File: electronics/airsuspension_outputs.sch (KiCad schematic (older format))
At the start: 51 parts, among them Q1 BSS138, Q2 BC847, U1 ITS5215L, U2 BTS6133D, U3 ITS5215L, U4 ITS5215L, U5 ITS5215L

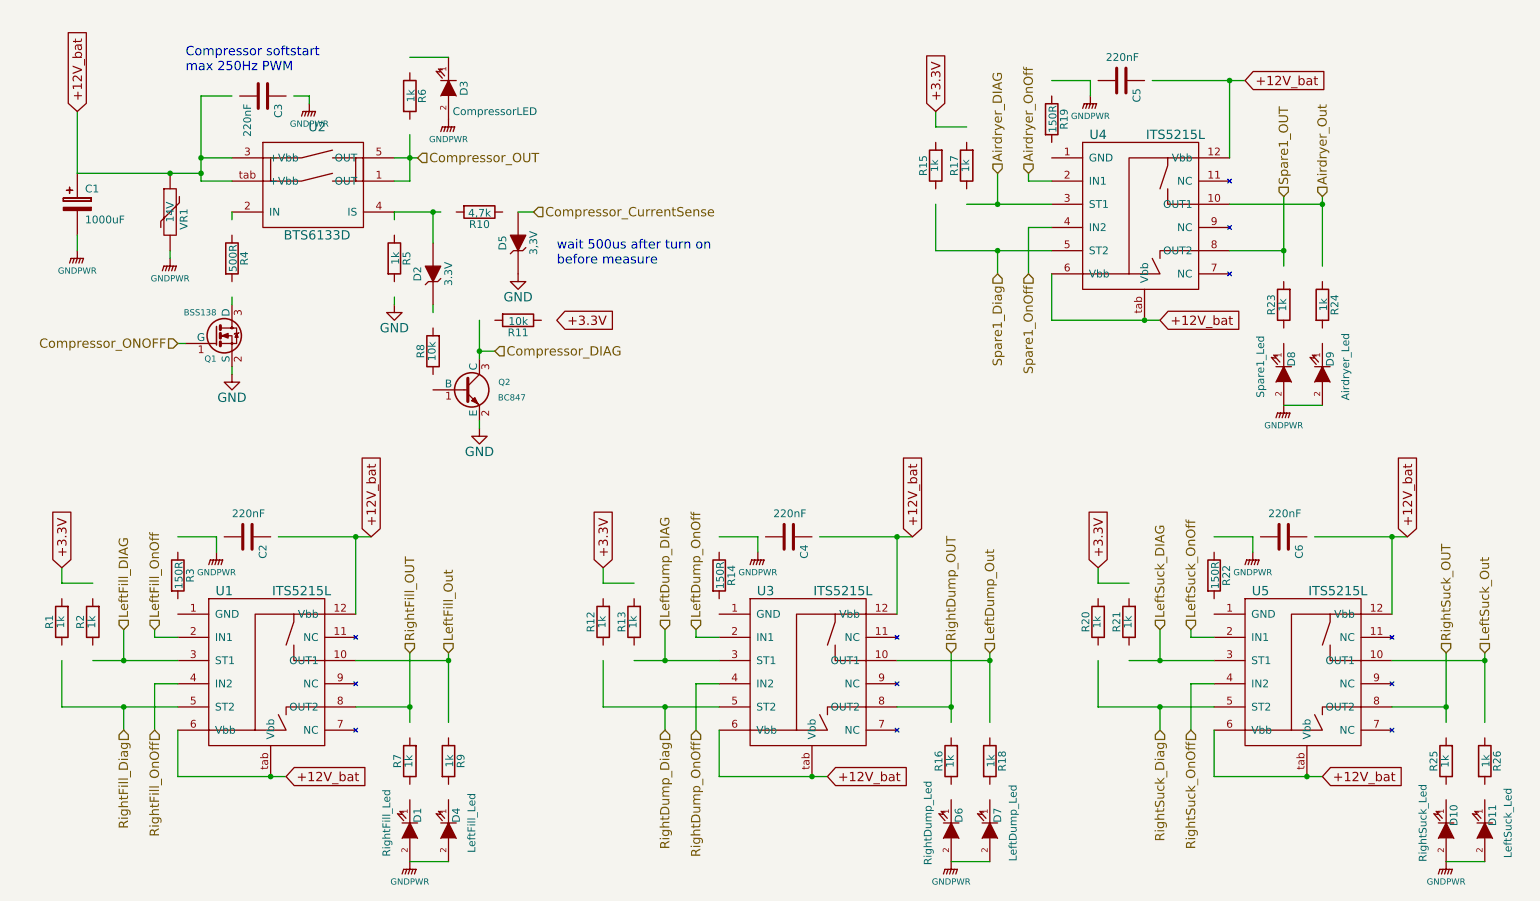
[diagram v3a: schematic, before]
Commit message: Changed to a more stable powersupply (3Amps 5V and separate 3.3v) + some few cleanups due to updated kicad
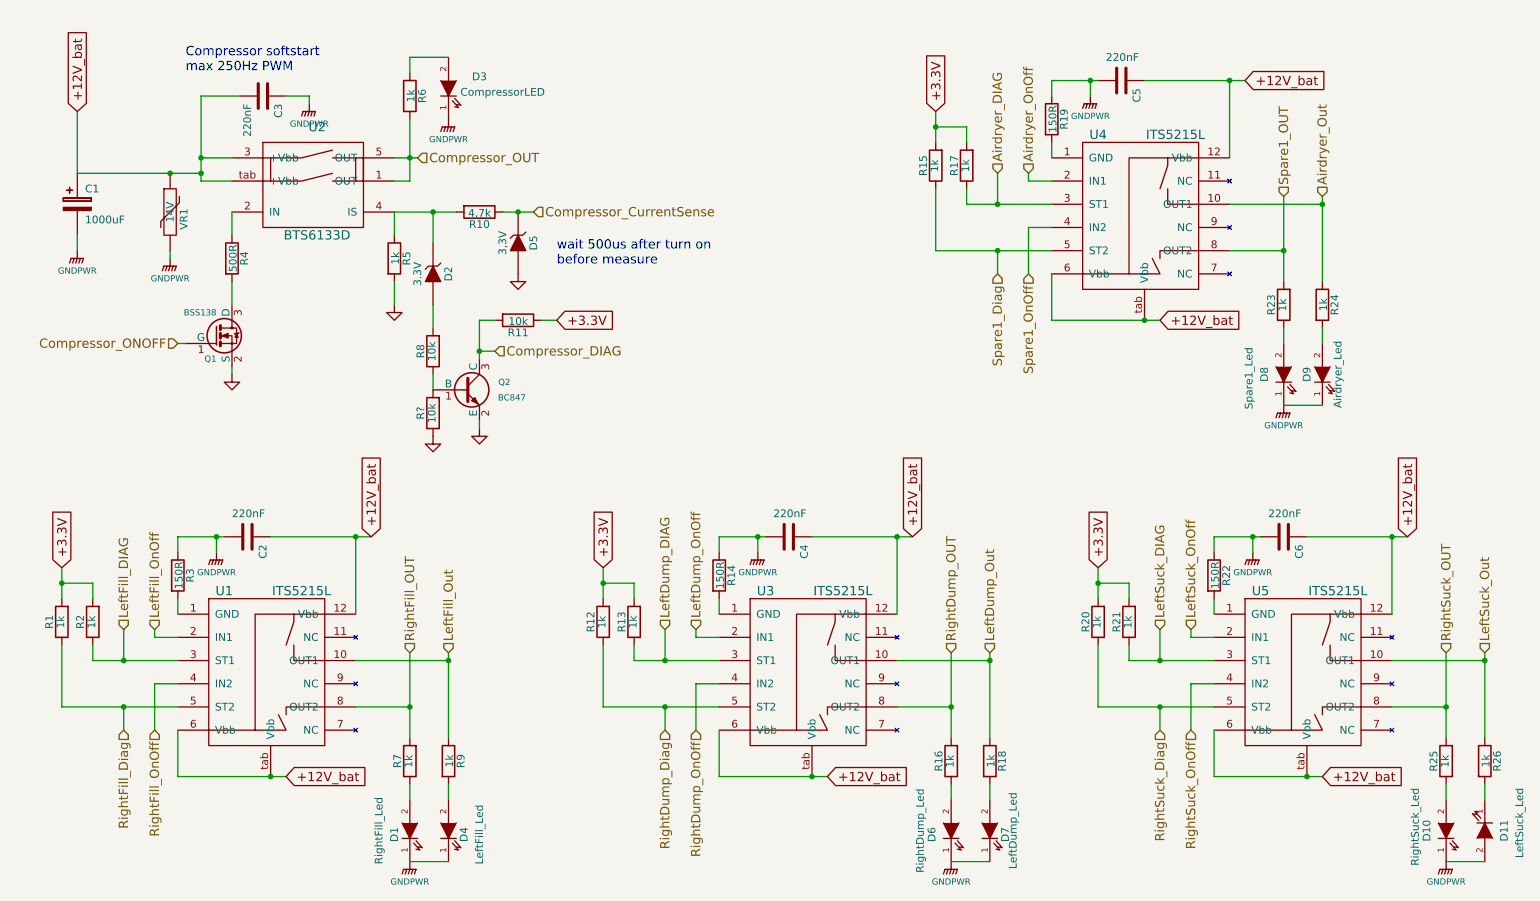
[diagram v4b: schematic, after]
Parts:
- added R?: 10k, Resistors_SMD:R_0805, symbol R
- U2: footprint SMD_Packages:DPAK-5 -> kicad_lib:bts6133d
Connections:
- wire segments 115 -> 143

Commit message: First placement with a ModICE enclosure
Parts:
- D1, D10, D11, D3, D4, D6, D7, D8, D9: footprint LEDs:LED-0805 -> LEDs:LED_0805
- Q1, Q2: footprint Housings_SOT-23_SOT-143_TSOT-6:SOT-23 -> TO_SOT_Packages_SMD:SOT-23_Handsoldering
- R54: renamed from R?; value 10k -> 1k; farnell 612522 -> 1577659; name CR0805-FX-1002ELF -> ERA6AEB102V
- R8: value 10k -> 1k; farnell 612522 -> 1577659; name CR0805-FX-1002ELF -> ERA6AEB102V
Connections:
- net GNDPWR: now also D11.1 (K); no longer D11.2 (A)
- net at R26.2: now also D11.2 (A); no longer D11.1 (K)
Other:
- note added: "wait 500us after turn on\nbefore current measure"
- note removed: "wait 500us after turn on\nbefore measure"
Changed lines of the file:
@@
 LIBS:power_switches
 LIBS:miscellaneous
+LIBS:cinch
 LIBS:airsuspension_controller-cache
 EELAYER 25 0
@@
 +12V_bat
 $Comp
-L GNDPWR #PWR06
+L GNDPWR #PWR07
 U 1 1 5504BD26
 P 3000 1150
-F 0 "#PWR06" H 3000 950 40  0001 C CNN
+F 0 "#PWR07" H 3000 950 40  0001 C CNN
 F 1 "GNDPWR" H 3000 1020 40  0000 C CNN
 F 2 "" H 3000 1100 60  0000 C CNN
@@
 $EndComp
 $Comp
-L GNDPWR #PWR07
+L GNDPWR #PWR08
 U 1 1 5504BD5A
 P 2100 2150
-F 0 "#PWR07" H 2100 1950 40  0001 C CNN
+F 0 "#PWR08" H 2100 1950 40  0001 C CNN
 F 1 "GNDPWR" H 2100 2020 40  0000 C CNN
 F 2 "" H 2100 2100 60  0000 C CNN
@@
 $EndComp
 $Comp
-L GNDPWR #PWR08
+L GNDPWR #PWR09
 U 1 1 5504BD7C
 P 1500 2100
-F 0 "#PWR08" H 1500 1900 40  0001 C CNN
+F 0 "#PWR09" H 1500 1900 40  0001 C CNN
 F 1 "GNDPWR" H 1500 1970 40  0000 C CNN
 F 2 "" H 1500 2050 60  0000 C CNN
@@
 $EndComp
 $Comp
-L GNDPWR #PWR09
+L GNDPWR #PWR010
 U 1 1 5504BE79
 P 2400 4050
-F 0 "#PWR09" H 2400 3850 40  0001 C CNN
+F 0 "#PWR010" H 2400 3850 40  0001 C CNN
 F 1 "GNDPWR" H 2400 3920 40  0000 C CNN
 F 2 "" H 2400 4000 60  0000 C CNN
@@
 $EndComp
 $Comp
-L GND #PWR010
+L GND #PWR011
 U 1 1 5504D3D3
 P 2500 2900
-F 0 "#PWR010" H 2500 2650 60  0001 C CNN
+F 0 "#PWR011" H 2500 2650 60  0001 C CNN
 F 1 "GND" H 2500 2750 60  0001 C CNN
 F 2 "" H 2500 2900 60  0000 C CNN
@@
 P 3800 2750
 F 0 "R8" V 3880 2750 50  0000 C CNN
-F 1 "10k" V 3807 2751 50  0000 C CNN
+F 1 "1k" V 3807 2751 50  0000 C CNN
 F 2 "Resistors_SMD:R_0805" V 3730 2750 30  0001 C CNN
 F 3 "" H 3800 2750 30  0000 C CNN
-F 4 "CR0805-FX-1002ELF" V 3800 2750 60  0001 C CNN "name"
-F 5 "612522" V 3800 2750 60  0001 C CNN "farnell"
+F 4 "ERA6AEB102V" V 3800 2750 60  0001 C CNN "name"
+F 5 "1577659" V 3800 2750 60  0001 C CNN "farnell"
 	1    3800 2750
 	-1   0    0    1
 $EndComp
 $Comp
-L GND #PWR011
+L GND #PWR012
 U 1 1 5504D6E9
 P 4100 3250
-F 0 "#PWR011" H 4100 3000 60  0001 C CNN
+F 0 "#PWR012" H 4100 3000 60  0001 C CNN
 F 1 "GND" H 4100 3100 60  0001 C CNN
 F 2 "" H 4100 3250 60  0000 C CNN
@@
 $EndComp
 $Comp
-L GND #PWR012
+L GND #PWR013
 U 1 1 5504D71D
 P 3550 2450
-F 0 "#PWR012" H 3550 2200 60  0001 C CNN
+F 0 "#PWR013" H 3550 2200 60  0001 C CNN
 F 1 "GND" H 3550 2300 60  0001 C CNN
 F 2 "" H 3550 2450 60  0000 C CNN
@@
 $EndComp
 $Comp
-L GND #PWR013
+L GND #PWR014
 U 1 1 5504DCBC
 P 4350 2250
-F 0 "#PWR013" H 4350 2000 60  0001 C CNN
+F 0 "#PWR014" H 4350 2000 60  0001 C CNN
 F 1 "GND" H 4350 2100 60  0001 C CNN
 F 2 "" H 4350 2250 60  0000 C CNN
@@
 F 0 "D3" V 3975 850 50  0000 C CNN
 F 1 "CompressorLED" V 3875 700 50  0000 C CNN
-F 2 "LEDs:LED-0805" H 3900 1050 60  0001 C CNN
+F 2 "LEDs:LED_0805" H 3900 1050 60  0001 C CNN
 F 3 "" H 3900 1050 60  0000 C CNN
 F 4 "KP-2012CGCK" H 3900 1050 60  0001 C CNN "name"
@@
 $EndComp
 $Comp
-L GNDPWR #PWR014
+L GNDPWR #PWR015
 U 1 1 5504E76C
 P 3900 1250
-F 0 "#PWR014" H 3900 1050 40  0001 C CNN
+F 0 "#PWR015" H 3900 1050 40  0001 C CNN
 F 1 "GNDPWR" H 3900 1120 40  0000 C CNN
 F 2 "" H 3900 1200 60  0000 C CNN
@@
 Compressor softstart\nmax 250Hz PWM
 Text Notes 4600 2200 0    60   ~ 0
-wait 500us after turn on\nbefore measure
+wait 500us after turn on\nbefore current measure
 $Comp
 L R R2
@@
 F 0 "D1" H 3625 5950 50  0000 C CNN
 F 1 "RightFill_Led" H 3650 6050 50  0000 C CNN
-F 2 "LEDs:LED-0805" H 3650 5850 60  0001 C CNN
+F 2 "LEDs:LED_0805" H 3650 5850 60  0001 C CNN
 F 3 "" H 3650 5850 60  0000 C CNN
 F 4 "KP-2012CGCK" H 3650 5850 60  0001 C CNN "name"
@@
 F 0 "D4" H 3875 5750 50  0000 C CNN
 F 1 "LeftFill_Led" H 3875 5650 50  0000 C CNN
-F 2 "LEDs:LED-0805" H 3900 5850 60  0001 C CNN
+F 2 "LEDs:LED_0805" H 3900 5850 60  0001 C CNN
 F 3 "" H 3900 5850 60  0000 C CNN
 F 4 "KP-2012CGCK" H 3900 5850 60  0001 C CNN "name"
@@
 $EndComp
 $Comp
-L GNDPWR #PWR015
+L GNDPWR #PWR016
 U 1 1 55050558
 P 3650 6050
-F 0 "#PWR015" H 3650 5850 40  0001 C CNN
+F 0 "#PWR016" H 3650 5850 40  0001 C CNN
 F 1 "GNDPWR" H 3650 5920 40  0000 C CNN
 F 2 "" H 3650 6000 60  0000 C CNN
@@
 $EndComp
 $Comp
-L GNDPWR #PWR016
+L GNDPWR #PWR017
 U 1 1 55056301
 P 8050 1100
-F 0 "#PWR016" H 8050 900 40  0001 C CNN
+F 0 "#PWR017" H 8050 900 40  0001 C CNN
 F 1 "GNDPWR" H 8050 970 40  0000 C CNN
 F 2 "" H 8050 1050 60  0000 C CNN
@@
 F 0 "D8" H 9300 3025 50  0000 C CNN
 F 1 "Spare1_Led" H 9275 3125 50  0000 C CNN
-F 2 "LEDs:LED-0805" H 9300 2900 60  0001 C CNN
+F 2 "LEDs:LED_0805" H 9300 2900 60  0001 C CNN
 F 3 "" H 9300 2900 60  0000 C CNN
 F 4 "2290331" H 9300 2900 60  0001 C CNN "farnell"
@@
 F 0 "D9" H 9550 3000 50  0000 C CNN
 F 1 "Airdryer_Led" H 9550 2800 50  0000 C CNN
-F 2 "LEDs:LED-0805" H 9550 2900 60  0001 C CNN
+F 2 "LEDs:LED_0805" H 9550 2900 60  0001 C CNN
 F 3 "" H 9550 2900 60  0000 C CNN
 F 4 "KP-2012CGCK" H 9550 2900 60  0001 C CNN "name"
@@
 $EndComp
 $Comp
-L GNDPWR #PWR017
+L GNDPWR #PWR018
 U 1 1 5505633E
 P 9300 3100
-F 0 "#PWR017" H 9300 2900 40  0001 C CNN
+F 0 "#PWR018" H 9300 2900 40  0001 C CNN
 F 1 "GNDPWR" H 9300 2970 40  0000 C CNN
 F 2 "" H 9300 3050 60  0000 C CNN
@@
 $EndComp
 $Comp
-L GNDPWR #PWR018
+L GNDPWR #PWR019
 U 1 1 5505681E
 P 9100 4050
-F 0 "#PWR018" H 9100 3850 40  0001 C CNN
+F 0 "#PWR019" H 9100 3850 40  0001 C CNN
 F 1 "GNDPWR" H 9100 3920 40  0000 C CNN
 F 2 "" H 9100 4000 60  0000 C CNN
@@
 F 0 "D10" H 10350 5975 50  0000 C CNN
 F 1 "RightSuck_Led" H 10375 6050 50  0000 C CNN
-F 2 "LEDs:LED-0805" H 10350 5850 60  0001 C CNN
+F 2 "LEDs:LED_0805" H 10350 5850 60  0001 C CNN
 F 3 "" H 10350 5850 60  0000 C CNN
 F 4 "2290331" H 10350 5850 60  0001 C CNN "farnell"
@@
 F 0 "D11" H 10600 5975 50  0000 C CNN
 F 1 "LeftSuck_Led" H 10550 6075 50  0000 C CNN
-F 2 "LEDs:LED-0805" H 10600 5850 60  0001 C CNN
+F 2 "LEDs:LED_0805" H 10600 5850 60  0001 C CNN
 F 3 "" H 10600 5850 60  0000 C CNN
 F 4 "KP-2012CGCK" H 10600 5850 60  0001 C CNN "name"
 F 5 "2290331" H 10600 5850 60  0001 C CNN "farnell"
 	1    10600 5850
-	0    1    1    0
-$EndComp
-$Comp
-L GNDPWR #PWR019
+	0    -1   -1   0
+$EndComp
+$Comp
+L GNDPWR #PWR020
 U 1 1 5505685B
 P 10350 6050
-F 0 "#PWR019" H 10350 5850 40  0001 C CNN
+F 0 "#PWR020" H 10350 5850 40  0001 C CNN
 F 1 "GNDPWR" H 10350 5920 40  0000 C CNN
 F 2 "" H 10350 6000 60  0000 C CNN
@@
 $EndComp
 $Comp
-L GNDPWR #PWR020
+L GNDPWR #PWR021
 U 1 1 55056A62
 P 5900 4050
-F 0 "#PWR020" H 5900 3850 40  0001 C CNN
+F 0 "#PWR021" H 5900 3850 40  0001 C CNN
 F 1 "GNDPWR" H 5900 3920 40  0000 C CNN
 F 2 "" H 5900 4000 60  0000 C CNN
@@
 F 0 "D6" H 7125 5975 50  0000 C CNN
 F 1 "RightDump_Led" H 7150 6050 50  0000 C CNN
-F 2 "LEDs:LED-0805" H 7150 5850 60  0001 C CNN
+F 2 "LEDs:LED_0805" H 7150 5850 60  0001 C CNN
 F 3 "" H 7150 5850 60  0000 C CNN
 F 4 "2290331" H 7150 5850 60  0001 C CNN "farnell"
@@
 F 0 "D7" H 7375 5750 50  0000 C CNN
 F 1 "LeftDump_Led" H 7400 5700 50  0000 C CNN
-F 2 "LEDs:LED-0805" H 7400 5850 60  0001 C CNN
+F 2 "LEDs:LED_0805" H 7400 5850 60  0001 C CNN
 F 3 "" H 7400 5850 60  0000 C CNN
 F 4 "KP-2012CGCK" H 7400 5850 60  0001 C CNN "name"
@@
 $EndComp
 $Comp
-L GNDPWR #PWR021
+L GNDPWR #PWR022
 U 1 1 55056A9F
 P 7150 6050
-F 0 "#PWR021" H 7150 5850 40  0001 C CNN
+F 0 "#PWR022" H 7150 5850 40  0001 C CNN
 F 1 "GNDPWR" H 7150 5920 40  0000 C CNN
 F 2 "" H 7150 6000 60  0000 C CNN
@@
 F 0 "Q2" H 4300 3050 40  0000 R CNN
 F 1 "BC847" H 4400 2950 40  0000 R CNN
-F 2 "Housings_SOT-23_SOT-143_TSOT-6:SOT-23" H 4250 2900 29  0001 C CNN
+F 2 "TO_SOT_Packages_SMD:SOT-23_Handsoldering" H 4250 2900 29  0001 C CNN
 F 3 "" H 4000 3000 60  0000 C CNN
 F 4 "1773609" H 4000 3000 60  0001 C CNN "farnell"
@@
 F 0 "Q1" H 2400 2501 40  0000 R CNN
 F 1 "BSS138" H 2400 2800 40  0000 R CNN
-F 2 "Housings_SOT-23_SOT-143_TSOT-6:SOT-23" H 2270 2752 29  0001 C CNN
+F 2 "TO_SOT_Packages_SMD:SOT-23_Handsoldering" H 2270 2752 29  0001 C CNN
 F 3 "" H 2400 2650 60  0000 C CNN
 F 4 "2053833" H 2400 2650 60  0001 C CNN "farnell"
@@
 	9300 2600 9300 2700
 $Comp
-L R R?
+L R R54
 U 1 1 56FAA483
 P 3800 3150
-F 0 "R?" V 3880 3150 50  0000 C CNN
-F 1 "10k" V 3807 3151 50  0000 C CNN
+F 0 "R54" V 3880 3150 50  0000 C CNN
+F 1 "1k" V 3807 3151 50  0000 C CNN
 F 2 "Resistors_SMD:R_0805" V 3730 3150 30  0001 C CNN
 F 3 "" H 3800 3150 30  0000 C CNN
-F 4 "CR0805-FX-1002ELF" V 3800 3150 60  0001 C CNN "name"
-F 5 "612522" V 3800 3150 60  0001 C CNN "farnell"
+F 4 "ERA6AEB102V" V 3800 3150 60  0001 C CNN "name"
+F 5 "1577659" V 3800 3150 60  0001 C CNN "farnell"
 	1    3800 3150
 	-1   0    0    1
 $EndComp
 $Comp
-L GND #PWR?
+L GND #PWR023
 U 1 1 56FAA639
 P 3800 3300
-F 0 "#PWR?" H 3800 3050 50  0001 C CNN
+F 0 "#PWR023" H 3800 3050 50  0001 C CNN
 F 1 "GND" H 3808 3127 50  0001 C CNN
 F 2 "" H 3800 3300 50  0000 C CNN

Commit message: PCB routing done
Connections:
- net GND: no longer Q1.2 (S)
- net GNDPWR: now also Q1.2 (S)
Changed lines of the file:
@@
-	1    0    0    -1
-$EndComp
-$Comp
-L GND #PWR011
-U 1 1 5504D3D3
-P 2500 2900
-F 0 "#PWR011" H 2500 2650 60  0001 C CNN
-F 1 "GND" H 2500 2750 60  0001 C CNN
-F 2 "" H 2500 2900 60  0000 C CNN
-F 3 "" H 2500 2900 60  0000 C CNN
-	1    2500 2900
 	1    0    0    -1
 $EndComp
@@
 	1    0    0    -1
 $EndComp
+$Comp
+L GNDPWR #PWR?
+U 1 1 5701DD89
+P 2500 2900
+F 0 "#PWR?" H 2500 2700 50  0001 C CNN
+F 1 "GNDPWR" H 2507 2974 50  0001 C CNN
+F 2 "" H 2500 2850 50  0000 C CNN
+F 3 "" H 2500 2850 50  0000 C CNN
+	1    2500 2900
+	1    0    0    -1
+$EndComp

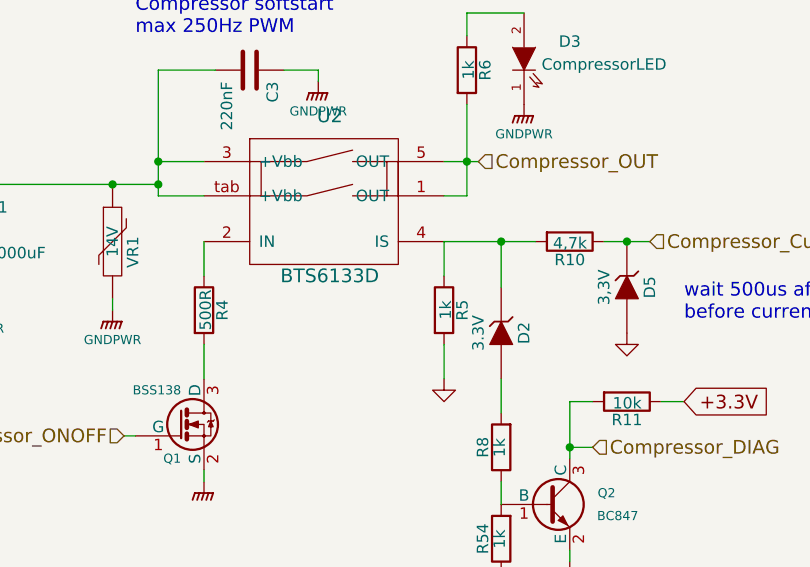
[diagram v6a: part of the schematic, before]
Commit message: Some updates as some parts were not available
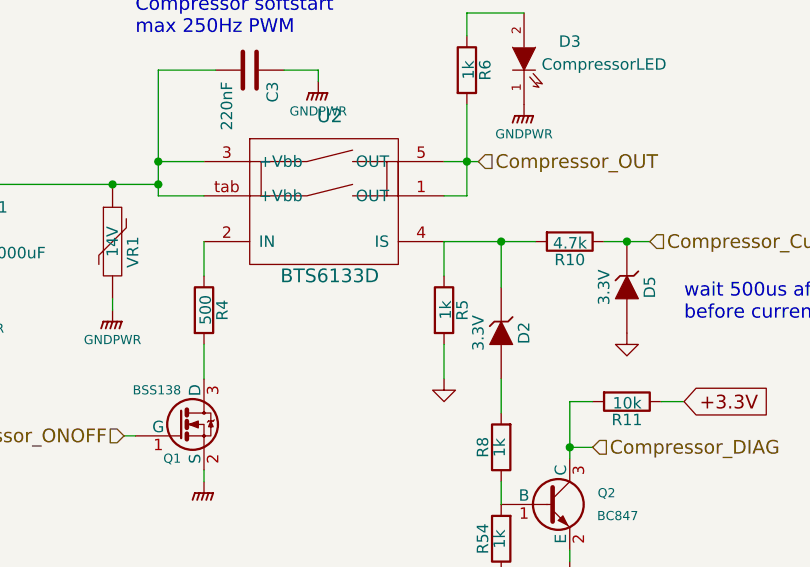
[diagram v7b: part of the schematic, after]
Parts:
- C1: name EEEFK1H102AM -> (none); part (none) -> EEEFK1H102AM
- C2, C3, C4, C5, C6: name C0805C224K5RACTU -> (none); part (none) -> C0805C224K5RACTU
- D1, D10, D11, D3, D4, D6, D7, D8, D9: name KP-2012CGCK -> (none); part (none) -> KP-2012CGCK
- D2: name PDZ3.3B,115 -> (none); part (none) -> PDZ3.3B.115
- D5: value 3,3V -> 3.3V; name PDZ3.3B,115 -> (none); part (none) -> PDZ3.3B.115
- Q1: name BSS138BK -> (none); part (none) -> BSS138BK
- Q2: name BC847C-7-F -> (none); part (none) -> BC847
- R1, R12, R13, R15, R16, R17, R18, R2, R20, R21, R23, R24, R25, R26, R5, R54, R7, R8, R9: farnell 1577659 -> 9332383; name ERA6AEB102V -> (none)
- R10: value 4,7k -> 4.7k; name CR0805-FX-4701ELF -> (none)
- R11: farnell 612522 -> 9332391; name CR0805-FX-1002ELF -> (none)
- R14, R19, R22, R3: farnell 2303460 -> 1469877; name ERJ6ENF1500V -> (none)
- R4: value 500R -> 500; farnell 2303491 -> 1469936; name ERJ6ENF3000V -> (none)
- R6: farnell (none) -> 9332383
- U1: name ITS5215L -> (none); part (none) -> ITS5215L
- U2: name BTS6133D -> (none); part (none) -> BTS6133D
- U3, U4, U5: part (none) -> ITS5215L
- VR1: name V14MLA1206NHAUTO -> (none); part (none) -> V14MLA1206NHAUTO
